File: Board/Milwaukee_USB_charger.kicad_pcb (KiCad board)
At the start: 2 copper layers, 61 x 74 mm, 37 parts, among them J1 BATT+, J2 BATT-, J3 USB_A_Stacked, J4 Barrel_Jack_Switch, Q1 Q_PMOS_GDS, Q2 Q_PMOS_GDS, U1 LM25085MY, U2 LM25085MY

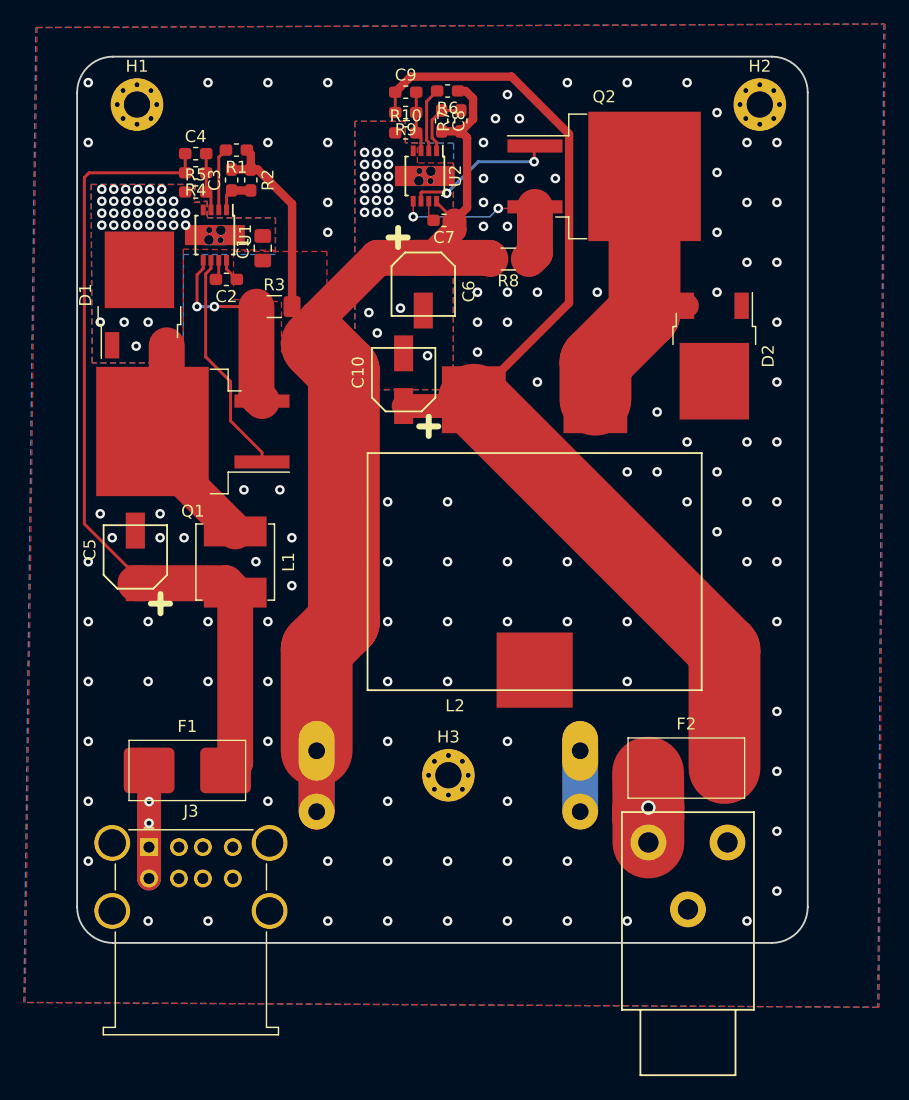
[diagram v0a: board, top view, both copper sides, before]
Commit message: Changed current measuring res, updated routing.
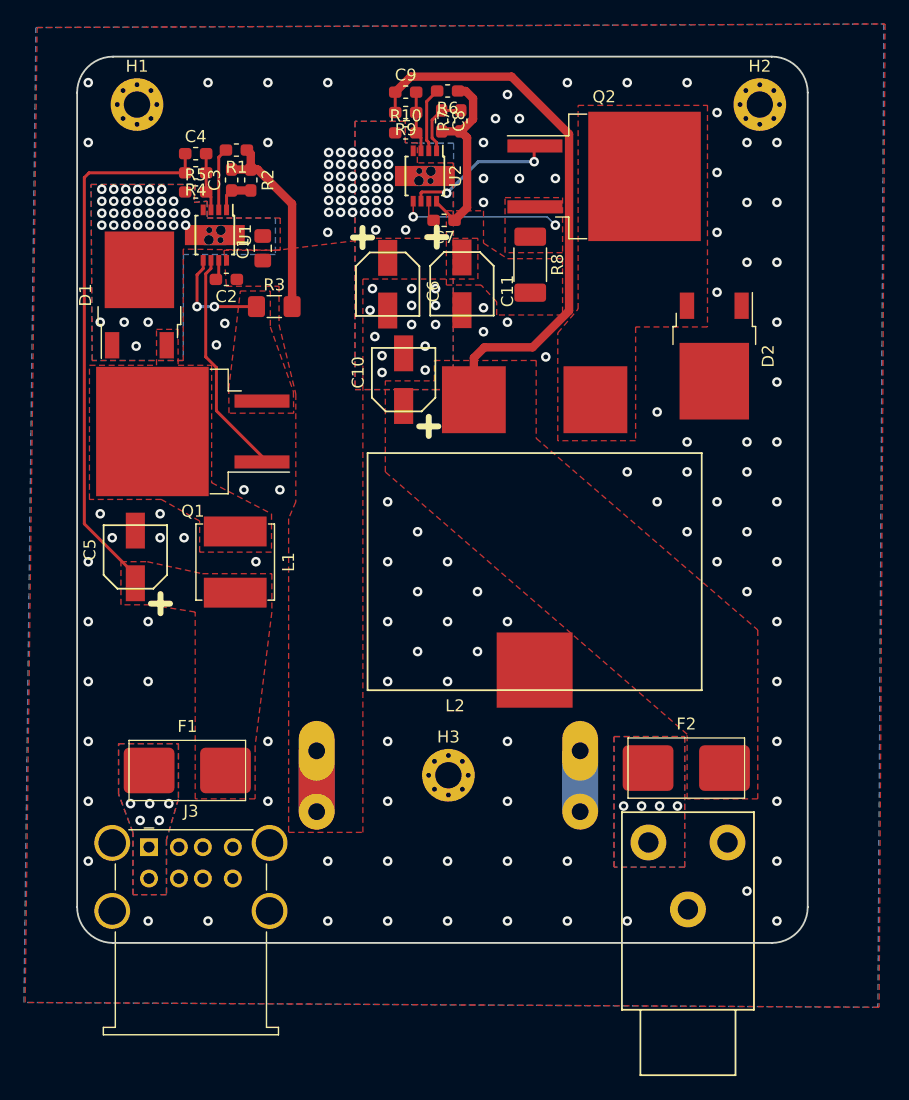
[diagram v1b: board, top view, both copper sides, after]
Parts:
- added C11: 47uF/25V, Capacitors:25SVPF47M, F.Cu at (101.1, 55.0)
- R8: value 10m -> 10m/1.5W; footprint Resistor_SMD:R_1206_3216Metric_Pad1.42x1.75mm_HandSolder -> Resistor_SMD:R_2010_5025Metric_Pad1.52x2.65mm_HandSolder
- moved C6 2.97 mm to (94.9, 55.0)
- moved R8 1.89 mm to (106.8, 53.4), turned to 270 degrees
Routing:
- net BATT+: track 99.2 -> 38.2 mm
- net Net-(C10-Pad1): track 89.7 -> 46.7 mm
- net Net-(D2-Pad3): track 24.1 -> 0.00 mm
- net Net-(C4-Pad1): track 69.6 -> 45.8 mm
- net +5V: track 19.2 -> 0.00 mm, vias 2 -> 5
- net Net-(D1-Pad3): track 18.9 -> 3.12 mm
- net +12V: track 8.75 -> 0.00 mm, vias 1 -> 4
- net Net-(Q1-Pad3): track 17.1 -> 9.04 mm
- net Net-(Q2-Pad3): track 16.4 -> 13.6 mm
- net GND: vias 171 -> 190
- added copper zone on B.Cu, net +12V
- added copper zone on F.Cu, net +12V
- added copper zone on B.Cu, net +5V
- added copper zone on F.Cu, net +5V
- added copper zone on F.Cu, net Net-(C10-Pad1)
- added copper zone on F.Cu, net Net-(C4-Pad1)
- added copper zone on F.Cu, net Net-(D1-Pad3)
- added copper zone on F.Cu, net Net-(D2-Pad3)
- added copper zone on F.Cu, net Net-(Q1-Pad3)
- added copper zone on F.Cu, net Net-(Q2-Pad3)

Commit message: REPLACE PREVIOUS COMMIT.
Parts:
- R3: value 10m -> 10m/0.5W

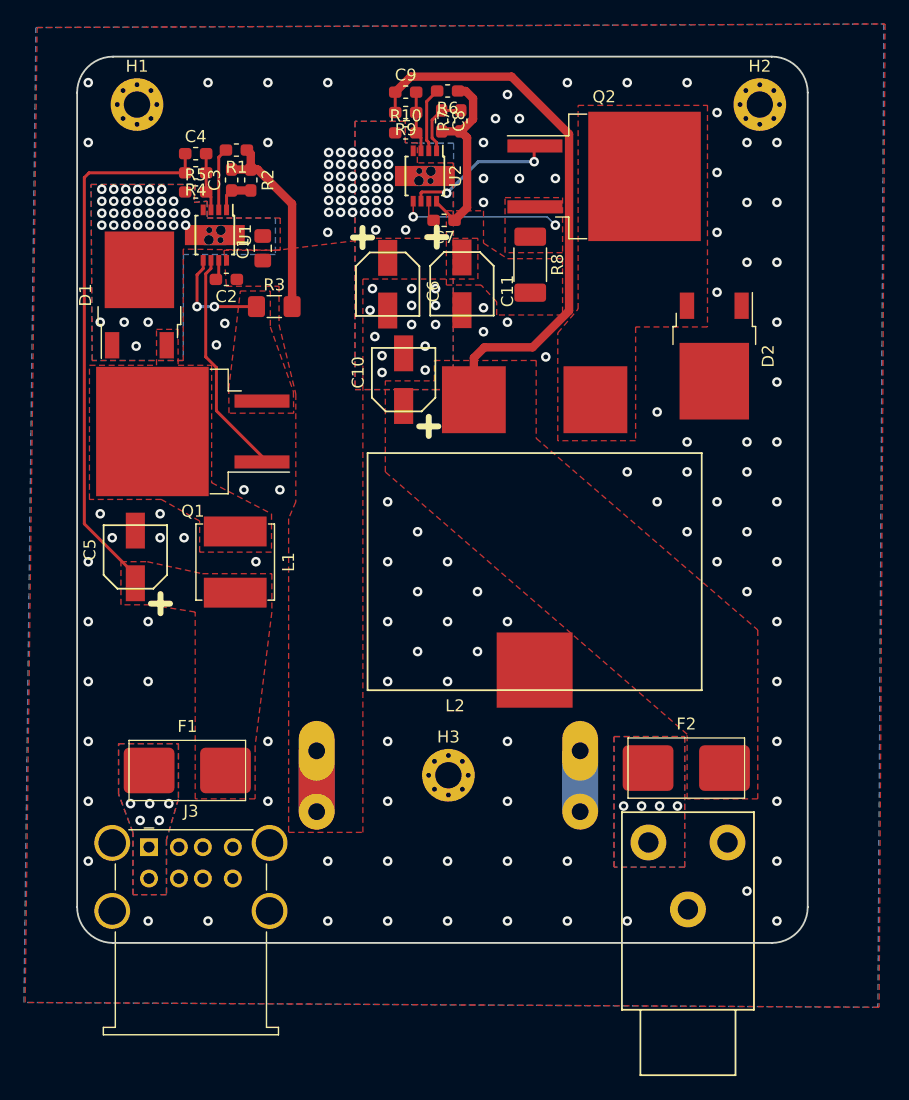
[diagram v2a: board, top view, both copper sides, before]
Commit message: Added one fuse and changed 10mOhm res to withstand 12A+
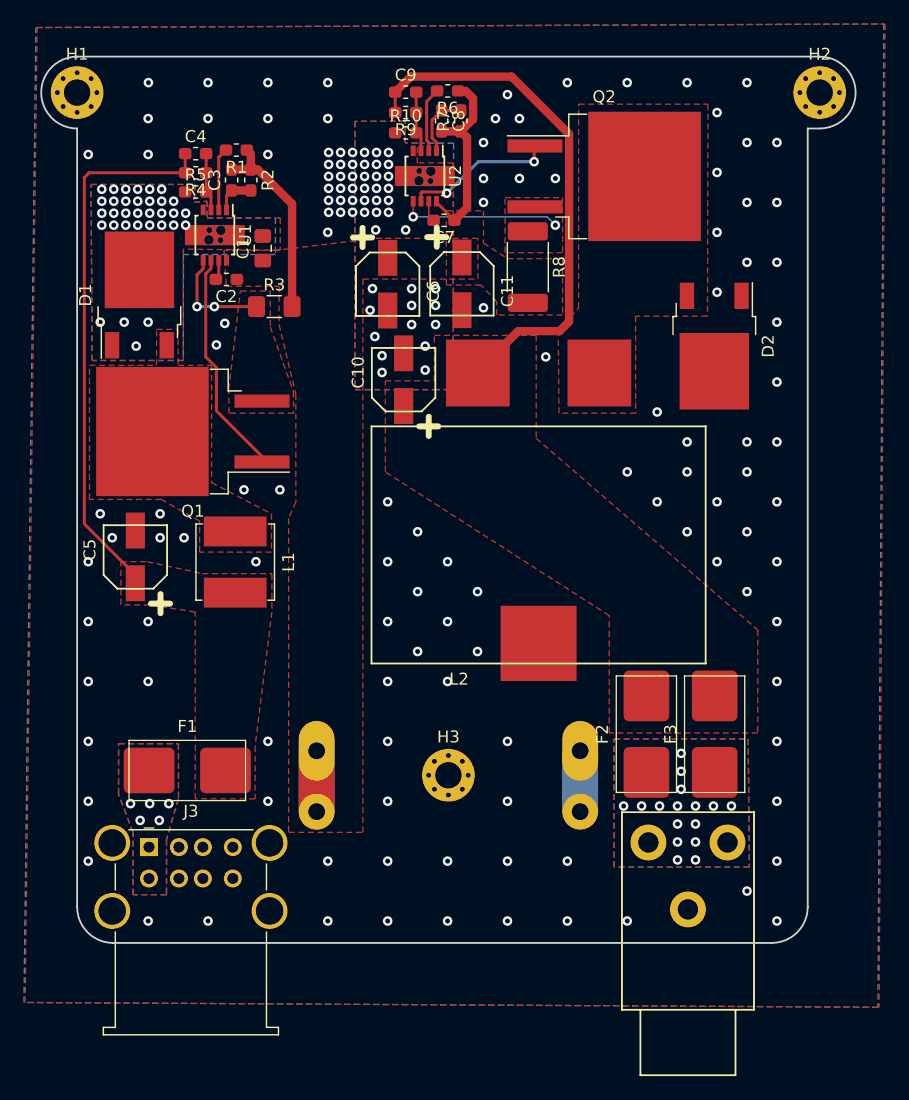
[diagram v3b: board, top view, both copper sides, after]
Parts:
- added F3: Fuse 7A, Fuses_custom:Fuse_holder_Littelfuse_154, F.Cu at (122.2, 92.6)
- F2: value Fuse 10A -> Fuse 7A
- R8: value 10m/1.5W -> 10m/2W; footprint Resistor_SMD:R_2010_5025Metric_Pad1.52x2.65mm_HandSolder -> Resistor_SMD:R_2512_6332Metric_Pad1.52x3.35mm_HandSolder
- moved H1 5.10 mm to (69.0, 39.0)
- moved H2 5.10 mm to (131.0, 39.0)
- moved F2 4.37 mm to (116.5, 92.6), turned to 90 degrees
- moved L2 2.25 mm to (107.5, 76.8)
- moved D2 0.83 mm to (122.2, 60.2)
- moved R8 0.28 mm to (106.6, 53.6)
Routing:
- net Net-(C10-Pad1): track 46.7 -> 44.0 mm
- net GND: vias 190 -> 193
- net +12V: vias 4 -> 16
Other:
- board size 61 x 74 mm -> 68 x 74 mm

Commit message: Updated silkscreen.
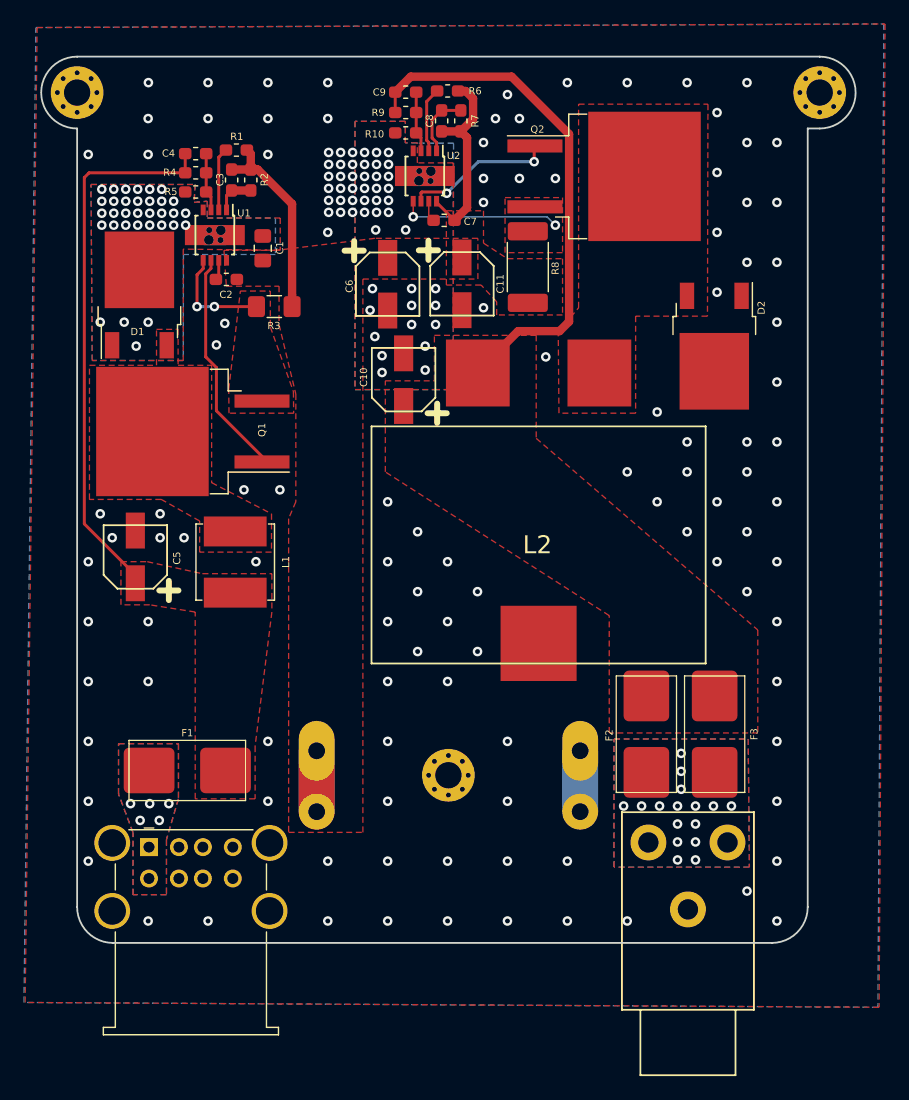
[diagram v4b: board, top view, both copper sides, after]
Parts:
- added G***: LOGO, Logos:taz, B.Cu at (100.0, 84.6)
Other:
- board text added: "Milwaukee_USB_charger_revA https://github.com/Talw3g/Milwaukee_USB_charger"

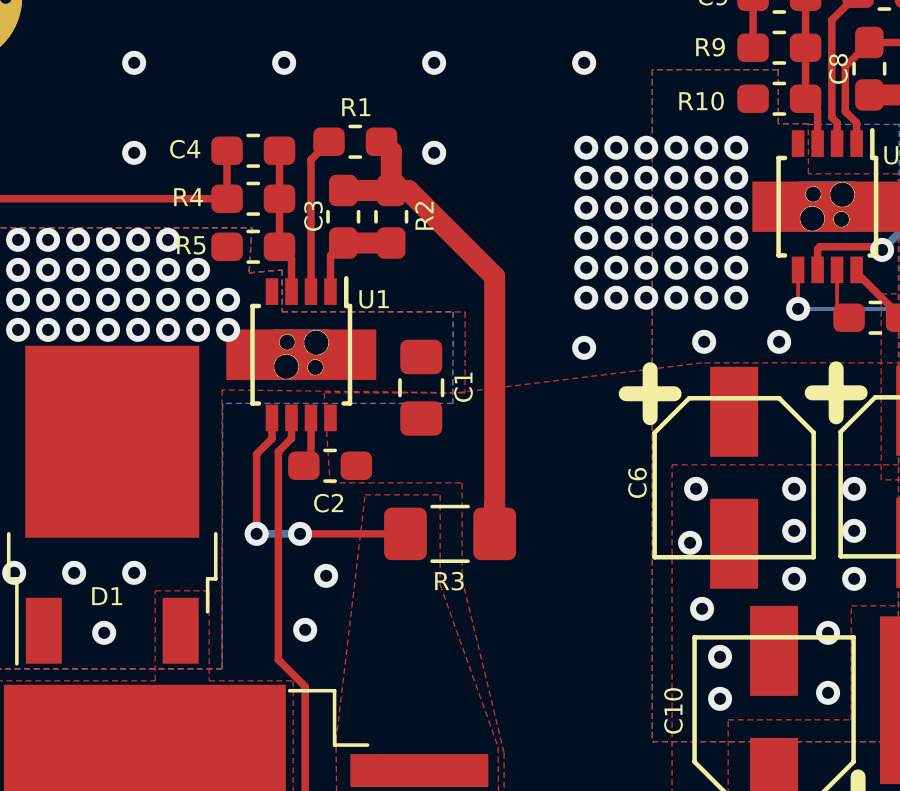
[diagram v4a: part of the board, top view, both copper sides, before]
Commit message: Used to 2W res instead of one 0.5W + one 2W
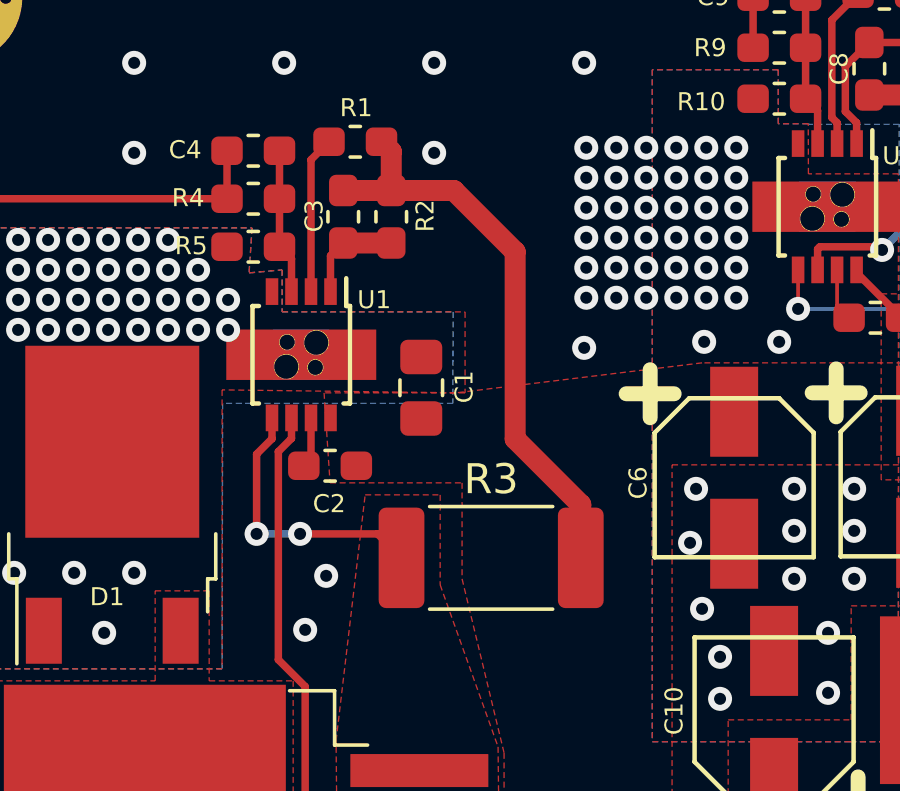
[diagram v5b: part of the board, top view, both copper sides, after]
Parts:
- removed G***: LOGO, Logos:taz
- R3: value 10m/0.5W -> 10m/2W; footprint Resistor_SMD:R_1206_3216Metric_Pad1.42x1.75mm_HandSolder -> Resistor_SMD:R_2512_6332Metric_Pad1.52x3.35mm_HandSolder
- moved R3 1.59 mm to (86.8, 57.7)
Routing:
- net BATT+: track 38.2 -> 41.1 mm

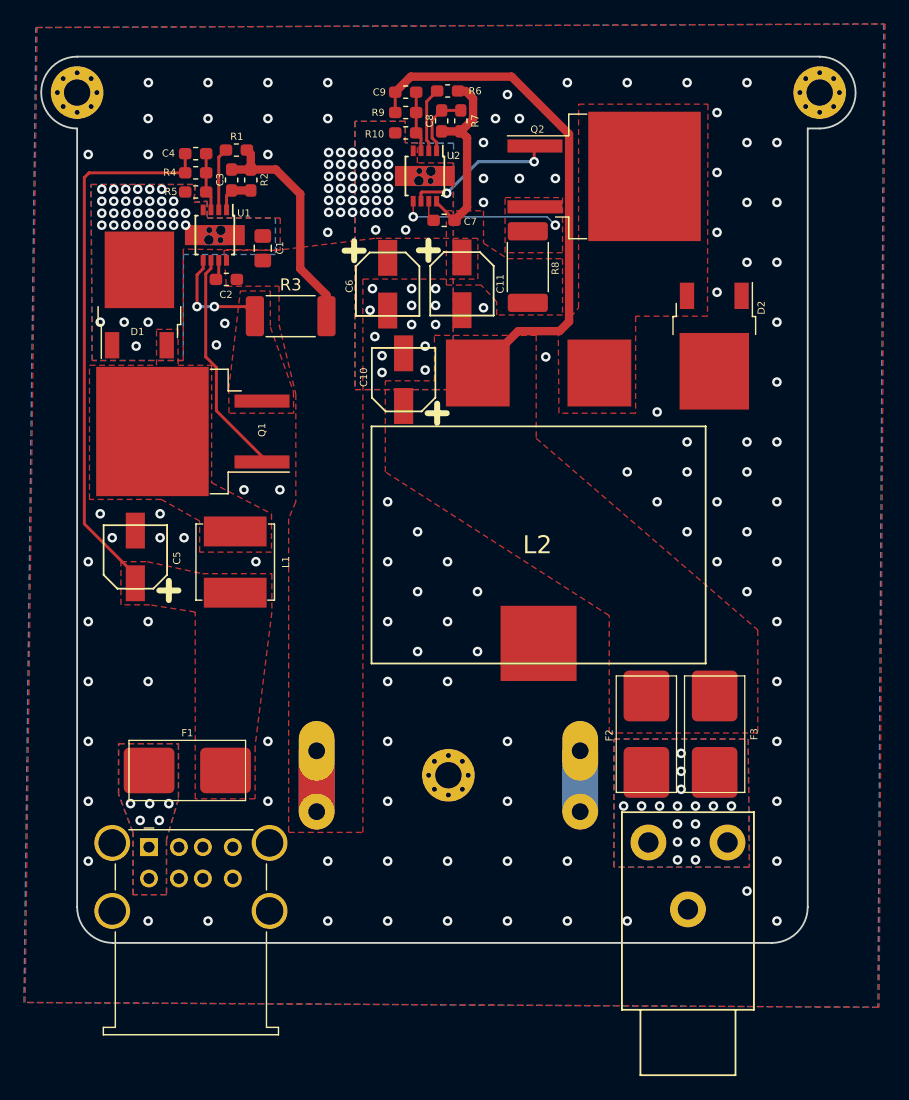
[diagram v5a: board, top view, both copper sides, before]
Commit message: /!\ Corrected schottky diode symbol !
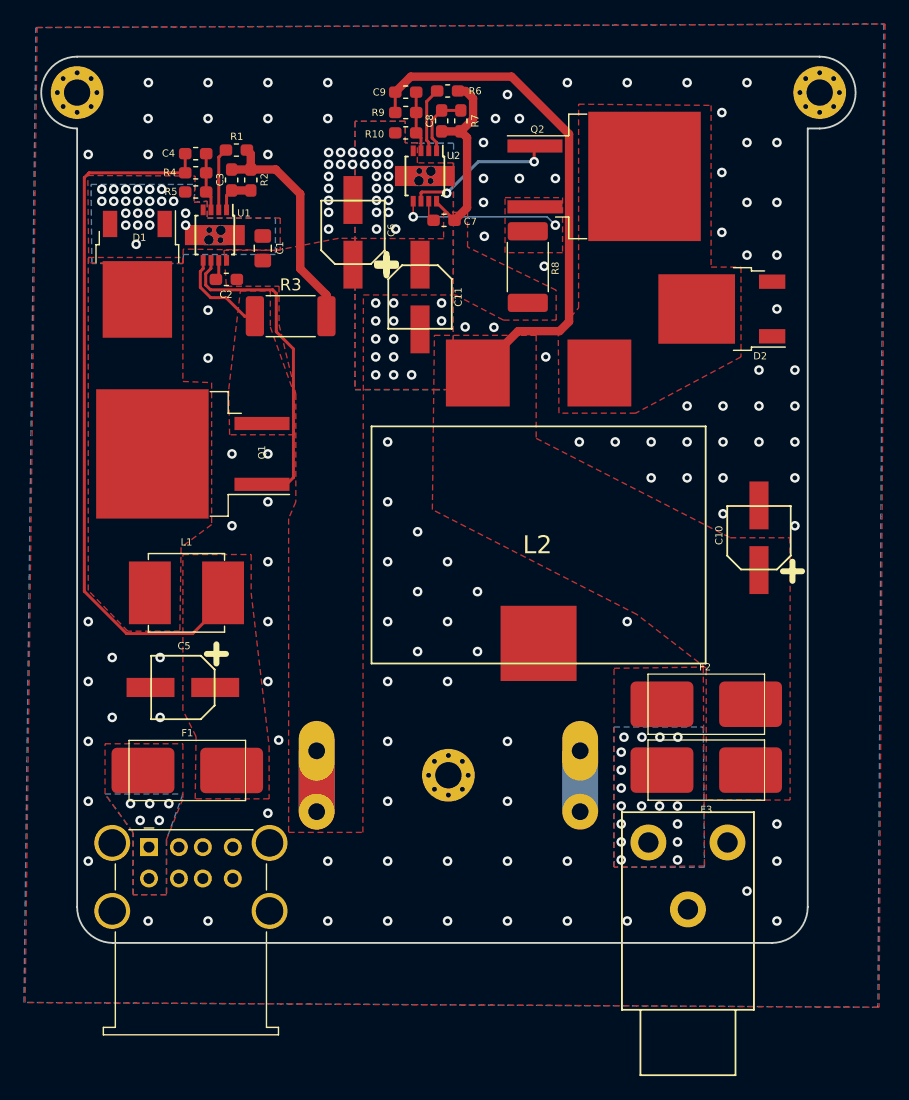
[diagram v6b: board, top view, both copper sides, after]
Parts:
- D1, D2: value D_Schottky_AAK -> D_Schottky_AKA
- moved C10 32.5 mm to (125.9, 76.2)
- moved C5 11.6 mm to (77.8, 88.7), turned to 90 degrees
- moved F2 5.59 mm to (121.5, 90.1), turned to 0 degrees
- moved C6 5.21 mm to (92.0, 50.7), turned to 0 degrees
- moved L1 4.81 mm to (78.1, 80.8), turned to 0 degrees
- moved C11 3.67 mm to (97.6, 56.1)
- moved D2 3.16 mm to (122.8, 57.1), turned to 180 degrees
- moved F3 3.08 mm to (121.5, 95.6), turned to 0 degrees
- moved Q1 1.87 mm to (78.7, 69.2)
- moved D1 1.74 mm to (74.0, 54.2), turned to 270 degrees
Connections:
- D1 pad 2: GND -> Net-(D1-Pad2)
- D1 pad 3: Net-(D1-Pad3) -> GND
- D2 pad 2: GND -> Net-(D2-Pad2)
- D2 pad 3: Net-(D2-Pad3) -> GND
- L1 pad 1: Net-(D1-Pad3) -> Net-(D1-Pad2)
- L2 pad 1: Net-(D2-Pad3) -> Net-(D2-Pad2)
- Q1 pad 2: Net-(D1-Pad3) -> Net-(D1-Pad2)
- Q2 pad 2: Net-(D2-Pad3) -> Net-(D2-Pad2)
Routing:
- net Net-(C4-Pad1): track 45.8 -> 59.7 mm
- net Net-(Q1-Pad1): track 19.0 -> 27.3 mm
- net Net-(D1-Pad3): track 3.12 -> 0.00 mm
- net Net-(D1-Pad2): track 0.00 -> 3.12 mm
- net Net-(Q1-Pad3): track 9.24 -> 7.91 mm, vias 2 -> 0
- net GND: vias 193 -> 174
- net +12V: vias 16 -> 17
- added copper zone on F.Cu, net Net-(D1-Pad2)
- added copper zone on F.Cu, net Net-(D2-Pad2)
- removed copper zone on F.Cu, net Net-(D1-Pad3)
- removed copper zone on F.Cu, net Net-(D2-Pad3)
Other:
- board text added: "Milwaukee_USB_charger_revB https://github.com/Talw3g/Milwaukee_USB_charger"
- board text removed: "Milwaukee_USB_charger_revA https://github.com/Talw3g/Milwaukee_USB_charger"
